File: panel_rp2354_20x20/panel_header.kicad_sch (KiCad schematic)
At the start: 4 parts, among them J2 Conn_01x05, J3 Conn_01x05, J4 Conn_01x05, J5 Conn_01x05

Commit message: Fixed part rotation issues.  Remove J2 J3 LCSC part as it was incorrect.
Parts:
- J2, J3: LCSC Part # C6585819 -> (none)
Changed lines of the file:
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@@
 			)
 		)
-		(property "LCSC Part #" "C6585819"
+		(property "LCSC Part #" ""
 			(at 99.695 90.805 0)
 			(effects
@@
 			)
 		)
-		(property "LCSC Part #" "C6585819"
+		(property "LCSC Part #" ""
 			(at 99.695 105.41 0)
 			(effects

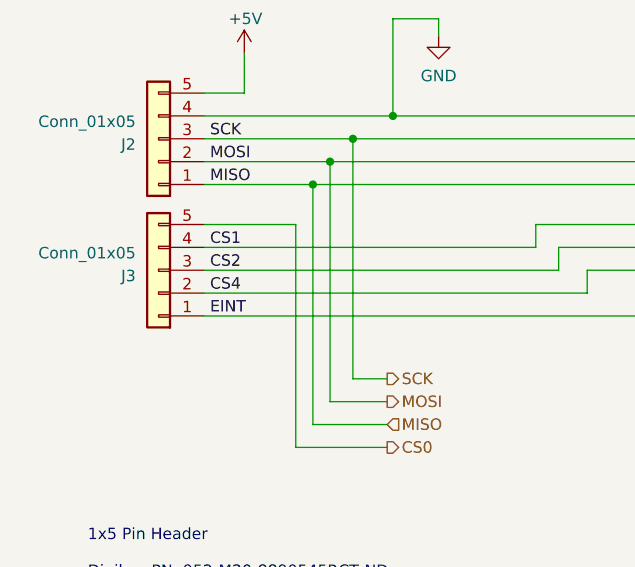
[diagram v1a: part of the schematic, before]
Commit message: Fixed net label issue ... changes CS3 to CS4.
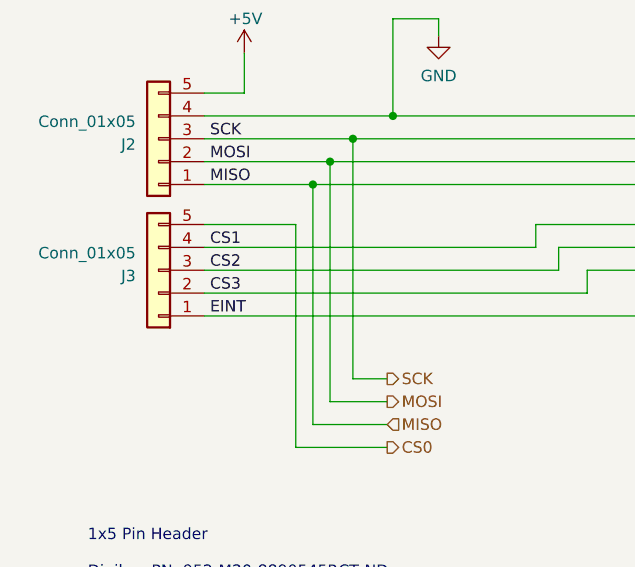
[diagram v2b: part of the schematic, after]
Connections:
- net CS4 renamed CS3
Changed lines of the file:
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@@
 		)
 	)
-	(label "CS4"
+	(label "CS3"
 		(at 105.41 107.95 0)
 		(effects
